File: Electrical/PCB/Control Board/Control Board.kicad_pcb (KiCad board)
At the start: 2 copper layers, 154 x 175 mm, 91 parts, among them J1 ED2627-ND, J10 6posheader, J11 S7038-ND, J13 ED1501-ND, J14 ED2989-ND-USB, J15 ED2580-ND, J16 ED2580-ND, J17 ED2744-ND, J18 ED2744-ND, J19 ED2744-ND, J2 ED2627-ND, J20 ED2744-ND, J21 ED2744-ND, J22 ED2744-ND, J23 ED2744-ND, J24 ED2744-ND, J25 ED2744-ND, J26 ED2744-ND, J28 ED2580-ND, J29 ED2580-ND, J3 ED2627-ND, J30 ED2580-ND, J31 ED2580-ND, J4 ED2627-ND, J5 ED2627-ND, J6 S9175-ND, J7 S9175-ND, J8 6posheader, J9 S7038-ND, M1 Mounting_Holes, T1 test_point, T10 test_point, T11 test_point, T12 test_point, T13 test_point, T14 test_point, T15 test_point, T16 test_point, T17 test_point, T18 test_point, T19 test_point, T2 test_point, T20 test_point, T21 test_point, T3 test_point, T4 test_point, T5 test_point, T6 test_point, T7 test_point, T8 test_point, T9 test_point, U1 LM358-N, U2 LM358-N, y1 rover_silkscreen

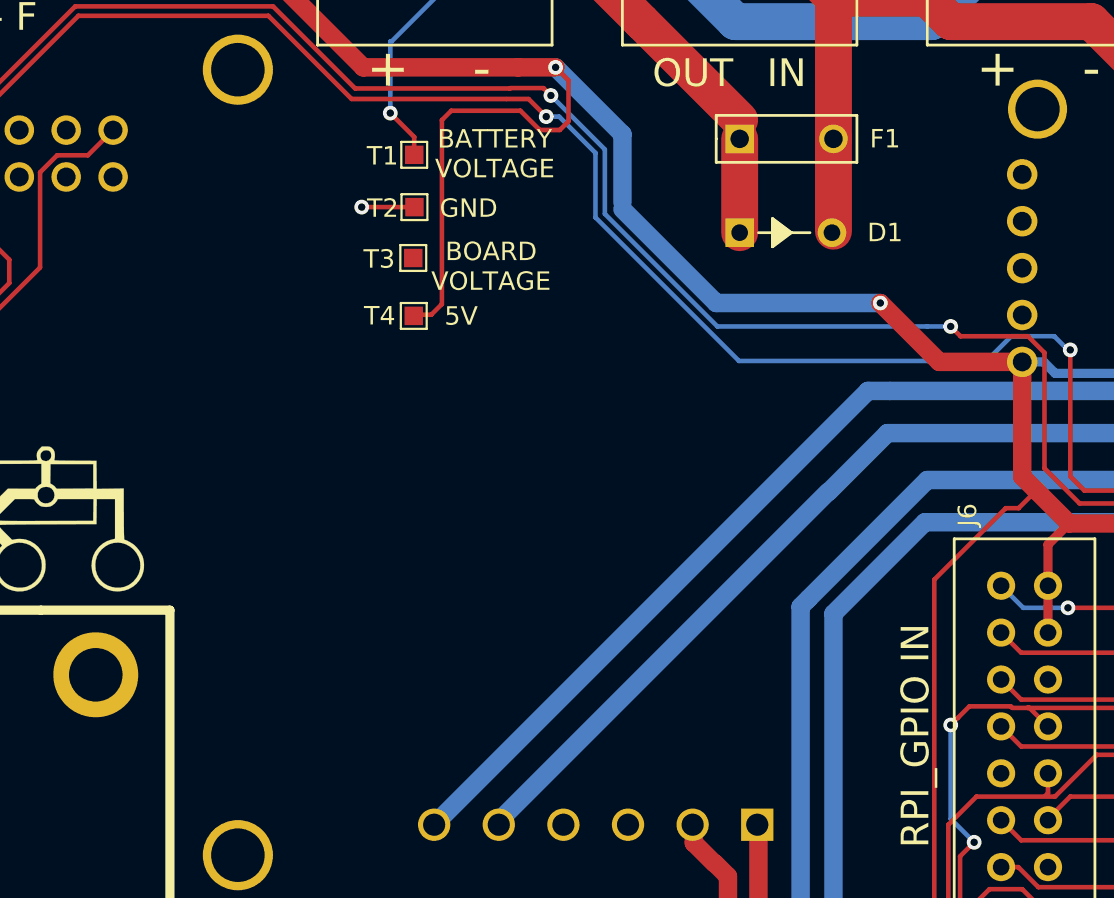
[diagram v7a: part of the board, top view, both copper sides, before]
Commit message: moved test points, added 3.3V decoupling capacitor
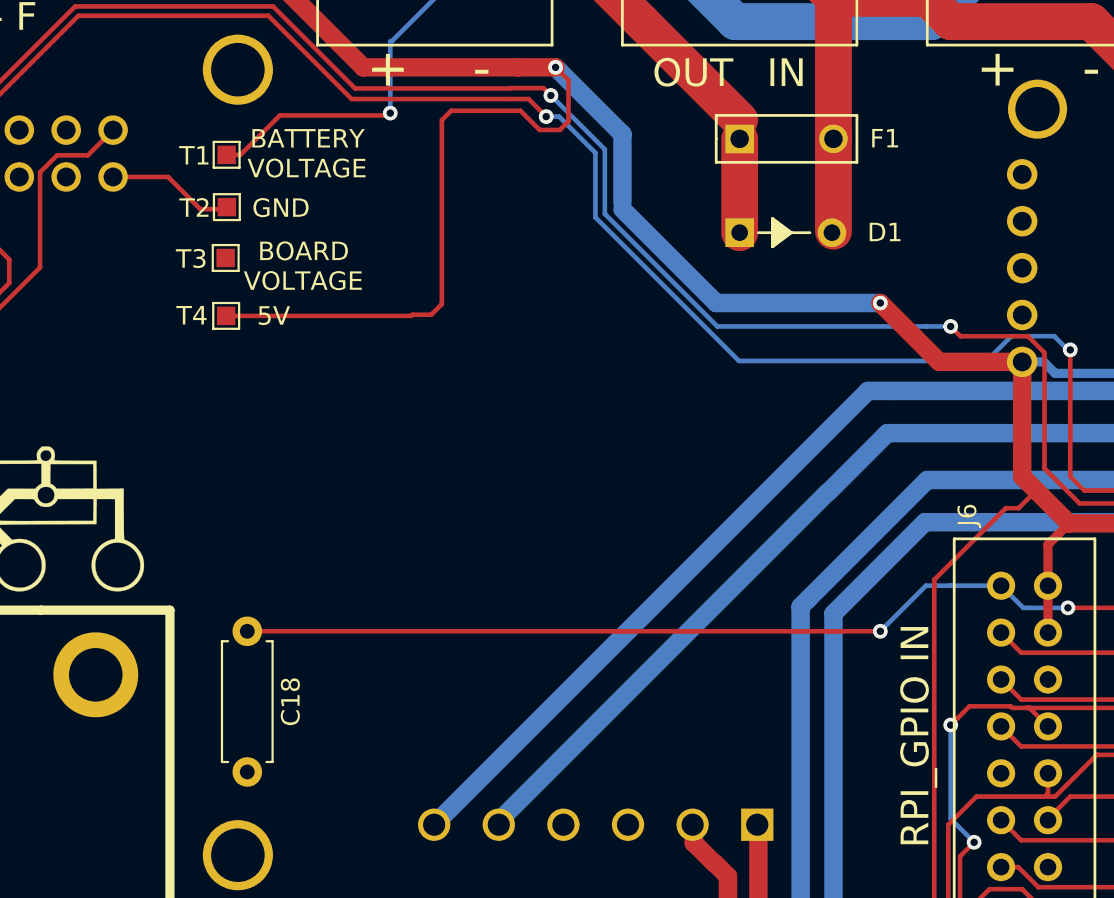
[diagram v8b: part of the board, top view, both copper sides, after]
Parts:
- added C18: 100nf, Resistor_THT:R_Axial_DIN0207_L6.3mm_D2.5mm_P7.62mm_Horizontal, F.Cu at (76.1, -128.3)
- moved T1 10.2 mm to (75.0, -154.1)
- moved T2 10.2 mm to (75.0, -151.3)
- moved T3 10.2 mm to (74.9, -148.6)
- moved T4 10.2 mm to (74.9, -145.4)
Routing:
- net /3.3V: track 53.8 -> 95.8 mm, vias 1 -> 2
- net +5V: track 1300.2 -> 1310.3 mm
- net Net-(D1-Pad1): track 37.5 -> 44.3 mm
- net GND: track 29.2 -> 33.0 mm, vias 2 -> 1
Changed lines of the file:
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@@
     (thickness 1.6)
     (drawings 172)
-    (tracks 1731)
+    (tracks 1743)
     (zones 0)
-    (modules 91)
+    (modules 92)
     (nets 184)
   )
@@
     (add_net "Net-(T14-Pad1)")
   )
+  (module Resistor_THT:R_Axial_DIN0207_L6.3mm_D2.5mm_P7.62mm_Horizontal (layer F.Cu)
+    (at 76.073 -128.3335 270)
+    (descr "Resistor, Axial_DIN0207 series, Axial, Horizontal, pin pitch=7.62mm, 0.25W = 1/4W, length*diameter=6.3*2.5mm^2, http://cdn-reichelt.de/documents/datenblatt/B400/1_4W%23YAG.pdf")
+    (tags "Resistor Axial_DIN0207 series Axial Horizontal pin pitch 7.62mm 0.25W = 1/4W length 6.3mm diameter 2.5mm")
+    (fp_text reference C18 (at 3.81 -2.37 90) (layer F.SilkS)
+      (effects (font (size 1 1) (thickness 0.15)))
+    )
+    (fp_text value 100nf (at 3.81 2.37 90) (layer F.Fab)
+      (effects (font (size 1 1) (thickness 0.15)))
+    )
+    (fp_text user %R (at 3.81 0 90) (layer F.Fab)
+      (effects (font (size 1 1) (thickness 0.15)))
+    )
+    (fp_line (start 8.67 -1.5) (end -1.05 -1.5) (layer F.CrtYd) (width 0.05))
+    (fp_line (start 8.67 1.5) (end 8.67 -1.5) (layer F.CrtYd) (width 0.05))
+    (fp_line (start -1.05 1.5) (end 8.67 1.5) (layer F.CrtYd) (width 0.05))
+    (fp_line (start -1.05 -1.5) (end -1.05 1.5) (layer F.CrtYd) (width 0.05))
+    (fp_line (start 7.08 1.37) (end 7.08 1.04) (layer F.SilkS) (width 0.12))
+    (fp_line (start 0.54 1.37) (end 7.08 1.37) (layer F.SilkS) (width 0.12))
+    (fp_line (start 0.54 1.04) (end 0.54 1.37) (layer F.SilkS) (width 0.12))
+    (fp_line (start 7.08 -1.37) (end 7.08 -1.04) (layer F.SilkS) (width 0.12))
+    (fp_line (start 0.54 -1.37) (end 7.08 -1.37) (layer F.SilkS) (width 0.12))
+    (fp_line (start 0.54 -1.04) (end 0.54 -1.37) (layer F.SilkS) (width 0.12))
+    (fp_line (start 7.62 0) (end 6.96 0) (layer F.Fab) (width 0.1))
+    (fp_line (start 0 0) (end 0.66 0) (layer F.Fab) (width 0.1))
+    (fp_line (start 6.96 -1.25) (end 0.66 -1.25) (layer F.Fab) (width 0.1))
+    (fp_line (start 6.96 1.25) (end 6.96 -1.25) (layer F.Fab) (width 0.1))
+    (fp_line (start 0.66 1.25) (end 6.96 1.25) (layer F.Fab) (width 0.1))
+    (fp_line (start 0.66 -1.25) (end 0.66 1.25) (layer F.Fab) (width 0.1))
+    (pad 2 thru_hole oval (at 7.62 0 270) (size 1.6 1.6) (drill 0.8) (layers *.Cu *.Mask)
+      (net 18 GND))
+    (pad 1 thru_hole circle (at 0 0 270) (size 1.6 1.6) (drill 0.8) (layers *.Cu *.Mask)
+      (net 127 /3.3V))
+    (model ${KISYS3DMOD}/Resistor_THT.3dshapes/R_Axial_DIN0207_L6.3mm_D2.5mm_P7.62mm_Horizontal.wrl
+      (at (xyz 0 0 0))
+      (scale (xyz 1 1 1))
+      (rotate (xyz 0 0 0))
+    )
+  )
   (module "JPL Robotics:ED2580-ND" (layer F.Cu)
     (at 83.693 -165.1635)
@@
   )
   (module TestPoint:TestPoint_Pad_1.0x1.0mm (layer F.Cu)
-    (at 85.09 -145.415)
+    (at 74.93 -145.415)
     (descr "SMD rectangular pad as test Point, square 1.0mm side length")
     (tags "test point SMD pad rectangle square")
@@
   )
   (module TestPoint:TestPoint_Pad_1.0x1.0mm (layer F.Cu)
-    (at 85.0646 -148.5519)
+    (at 74.9046 -148.5519)
     (descr "SMD rectangular pad as test Point, square 1.0mm side length")
     (tags "test point SMD pad rectangle square")
@@
   )
   (module TestPoint:TestPoint_Pad_1.0x1.0mm (layer F.Cu)
-    (at 85.1281 -151.3078)
+    (at 74.9681 -151.3078)
     (descr "SMD rectangular pad as test Point, square 1.0mm side length")
     (tags "test point SMD pad rectangle square")
@@
   )
   (module TestPoint:TestPoint_Pad_1.0x1.0mm (layer F.Cu)
-    (at 85.1154 -154.1399)
+    (at 74.9554 -154.1399)
     (descr "SMD rectangular pad as test Point, square 1.0mm side length")
     (tags "test point SMD pad rectangle square")
@@
     (effects (font (size 1.5 1.5) (thickness 0.3)))
   )
-  (gr_text 5V (at 87.6554 -145.4023) (layer F.SilkS)
+  (gr_text 5V (at 77.4954 -145.4023) (layer F.SilkS)
     (effects (font (size 1 1) (thickness 0.1)))
   )
-  (gr_text "BOARD\nVOLTAGE" (at 89.281 -148.0947) (layer F.SilkS)
+  (gr_text "BOARD\nVOLTAGE" (at 79.121 -148.0947) (layer F.SilkS)
     (effects (font (size 1 1) (thickness 0.1)))
   )
-  (gr_text GND (at 88.0618 -151.2443) (layer F.SilkS)
+  (gr_text GND (at 77.9018 -151.2443) (layer F.SilkS)
     (effects (font (size 1 1) (thickness 0.1)))
   )
-  (gr_text "BATTERY\nVOLTAGE" (at 89.4842 -154.1907) (layer F.SilkS)
+  (gr_text "BATTERY\nVOLTAGE" (at 79.3242 -154.1907) (layer F.SilkS)
     (effects (font (size 1 1) (thickness 0.1)))
   )
@@
   (via (at 89.3826 -12.9794) (size 0.8) (drill 0.4) (layers F.Cu B.Cu) (net 18))
   (segment (start 89.3826 -11.3284) (end 89.3826 -12.9794) (width 0.25) (layer F.Cu) (net 18))
-  (via (at 82.2706 -151.3078) (size 0.8) (drill 0.4) (layers F.Cu B.Cu) (net 18))
-  (segment (start 85.1281 -151.3078) (end 82.2706 -151.3078) (width 0.25) (layer F.Cu) (net 18))
   (segment (start 137.263 -7.6835) (end 135.763 -7.6835) (width 2) (layer B.Cu) (net 18))
   (segment (start 138.303 -165.1635) (end 138.303 -167.7035) (width 2) (layer B.Cu) (net 18))
+  (segment (start 68.805 -152.94) (end 71.7865 -152.94) (width 0.25) (layer F.Cu) (net 18))
+  (segment (start 71.7865 -152.94) (end 73.533 -151.1935) (width 0.25) (layer F.Cu) (net 18))
+  (segment (start 73.533 -151.1935) (end 74.803 -151.1935) (width 0.25) (layer F.Cu) (net 18))
   (via (at -0.0635 -113.03) (size 0.8) (drill 0.4) (layers F.Cu B.Cu) (net 19))
   (segment (start 7.1755 -118.7785) (end 5.685 -118.7785) (width 0.25) (layer B.Cu) (net 19))
@@
   (segment (start 113.553 -142.9235) (end 118.0465 -142.9235) (width 1) (layer F.Cu) (net 23))
   (segment (start 110.363 -146.1135) (end 113.553 -142.9235) (width 1) (layer F.Cu) (net 23))
+  (segment (start 84.963 -145.415) (end 85.0265 -145.4785) (width 0.25) (layer F.Cu) (net 23))
+  (segment (start 74.93 -145.415) (end 84.963 -145.415) (width 0.25) (layer F.Cu) (net 23))
   (via (at 115.443 -116.9035) (size 0.8) (drill 0.4) (layers F.Cu B.Cu) (net 24))
   (via (at 114.173 -123.2535) (size 0.8) (drill 0.4) (layers F.Cu B.Cu) (net 24))
@@
   (segment (start 129.722999 -108.910001) (end 131.579501 -108.910001) (width 0.25) (layer F.Cu) (net 127))
   (segment (start 128.27 -110.363) (end 129.722999 -108.910001) (width 0.25) (layer F.Cu) (net 127))
+  (segment (start 114.246 -130.8005) (end 112.83 -130.8005) (width 0.25) (layer B.Cu) (net 127))
+  (segment (start 116.9035 -130.8005) (end 114.246 -130.8005) (width 0.25) (layer B.Cu) (net 127))
+  (segment (start 114.246 -130.8005) (end 114.1 -130.8005) (width 0.25) (layer B.Cu) (net 127))
+  (segment (start 112.83 -130.8005) (end 110.363 -128.3335) (width 0.25) (layer B.Cu) (net 127))
+  (segment (start 110.363 -128.3335) (end 110.363 -128.3335) (width 0.25) (layer B.Cu) (net 127))
+  (via (at 110.363 -128.3335) (size 0.8) (drill 0.4) (layers F.Cu B.Cu) (net 127))
+  (segment (start 110.363 -128.3335) (end 76.073 -128.3335) (width 0.25) (layer F.Cu) (net 127))
   (segment (start 127.300499 -127.173499) (end 127.508001 -127.381001) (width 0.25) (layer F.Cu) (net 128))
   (segment (start 117.990501 -127.173499) (end 127.300499 -127.173499) (width 0.25) (layer F.Cu) (net 128))
@@
   (segment (start 25.273 -166.6635) (end 28.853 -170.2435) (width 2) (layer B.Cu) (net 180))
   (segment (start 25.273 -165.1635) (end 25.273 -166.6635) (width 2) (layer B.Cu) (net 180))
-  (via (at 83.82 -156.4005) (size 0.8) (drill 0.4) (layers F.Cu B.Cu) (net 183))
-  (segment (start 83.82 -160.274) (end 83.82 -156.4005) (width 0.25) (layer B.Cu) (net 183))
-  (segment (start 85.1154 -155.1051) (end 85.1154 -154.1399) (width 0.25) (layer F.Cu) (net 183))
-  (segment (start 83.82 -156.4005) (end 85.1154 -155.1051) (width 0.25) (layer F.Cu) (net 183))
-  (segment (start 102.743 -156.0285) (end 102.743 -155.0035) (width 0.25) (layer F.Cu) (net 183))
-  (segment (start 97.418 -161.3535) (end 102.743 -156.0285) (width 2) (layer F.Cu) (net 183))
-  (segment (start 102.743 -155.0035) (end 102.743 -149.9235) (width 2) (layer F.Cu) (net 183))
   (segment (start 116.713 -170.2435) (end 121.793 -165.1635) (width 2) (layer F.Cu) (net 181))
   (segment (start 93.853 -170.2435) (end 116.713 -170.2435) (width 2) (layer F.Cu) (net 181))
@@
   (segment (start 100.203 -163.6635) (end 102.513 -161.3535) (width 2) (layer B.Cu) (net 182))
   (segment (start 100.203 -165.1635) (end 100.203 -163.6635) (width 2) (layer B.Cu) (net 182))
+  (segment (start 83.82 -160.274) (end 83.82 -156.4005) (width 0.25) (layer B.Cu) (net 183))
+  (segment (start 102.743 -156.0285) (end 102.743 -155.0035) (width 0.25) (layer F.Cu) (net 183))
+  (segment (start 97.418 -161.3535) (end 102.743 -156.0285) (width 2) (layer F.Cu) (net 183))
+  (segment (start 102.743 -155.0035) (end 102.743 -149.9235) (width 2) (layer F.Cu) (net 183))
   (segment (start 83.8835 -160.274) (end 88.773 -165.1635) (width 0.25) (layer B.Cu) (net 183))
   (segment (start 83.82 -160.274) (end 83.8835 -160.274) (width 0.25) (layer B.Cu) (net 183))
   (segment (start 93.608 -165.1635) (end 97.418 -161.3535) (width 2) (layer F.Cu) (net 183))
   (segment (start 88.773 -165.1635) (end 93.608 -165.1635) (width 2) (layer F.Cu) (net 183))
+  (segment (start 83.82 -156.4005) (end 83.82 -156.4005) (width 0.25) (layer B.Cu) (net 183))
+  (via (at 83.82 -156.4005) (size 0.8) (drill 0.4) (layers F.Cu B.Cu) (net 183))
+  (segment (start 75.7054 -154.1399) (end 77.839 -156.2735) (width 0.25) (layer F.Cu) (net 183))
+  (segment (start 74.9554 -154.1399) (end 75.7054 -154.1399) (width 0.25) (layer F.Cu) (net 183))
+  (segment (start 77.839 -156.2735) (end 83.693 -156.2735) (width 0.25) (layer F.Cu) (net 183))
   (zone (net 26) (net_name +BATT) (layer F.Cu) (hatch edge 0.508)
     (connect_pads (clearance 0.508))
